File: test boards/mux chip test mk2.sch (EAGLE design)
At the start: 39 parts, among them IC1 741G3157DRLR, IC2 74AHC1G125DBV, IC3 741G3157DRLR, SW1 SPST_TACT-KMR2, U1 ATMEGA168MLF, Y1 16MHZ

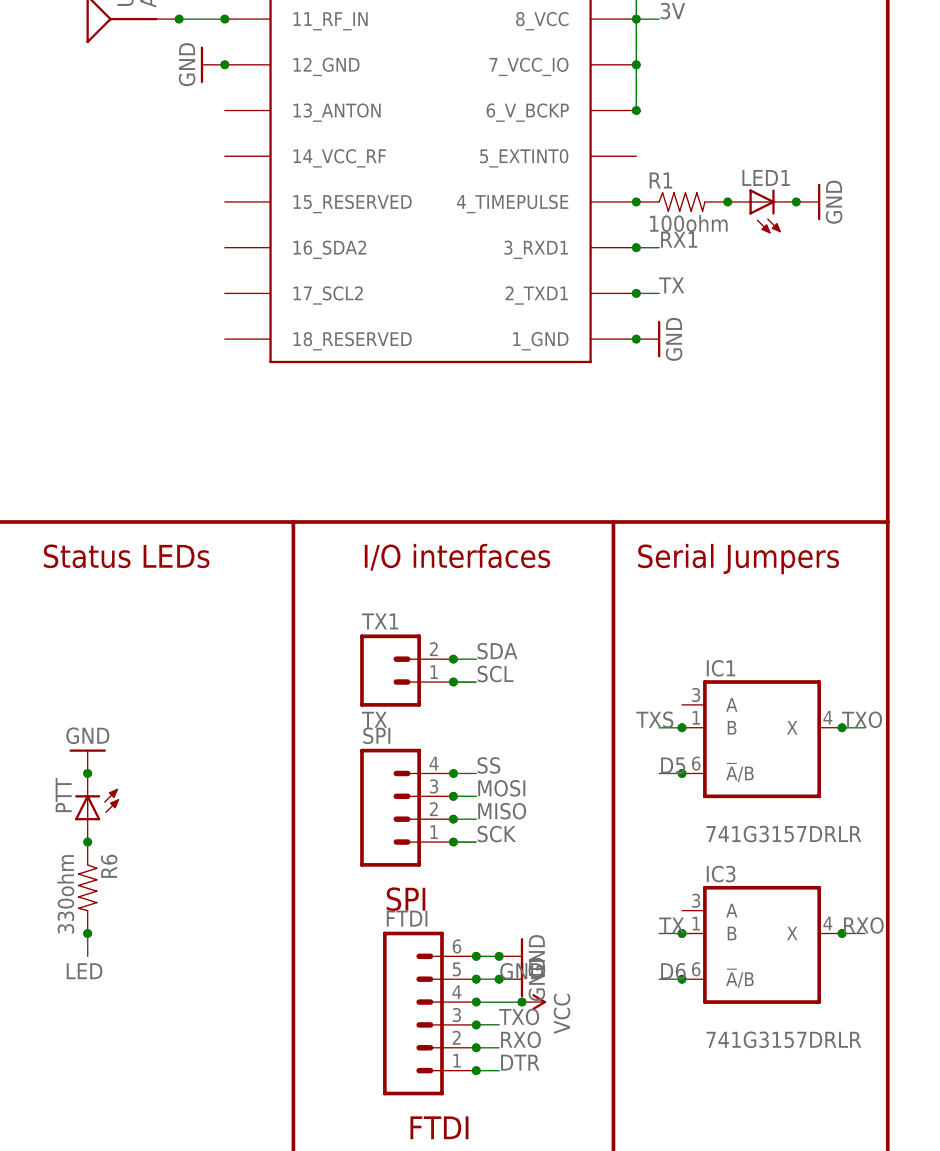
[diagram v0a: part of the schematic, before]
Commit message: Moved mix test LED
changed the schematic on the mux test to move the pulse per second LED
to the correct area on the schematic.
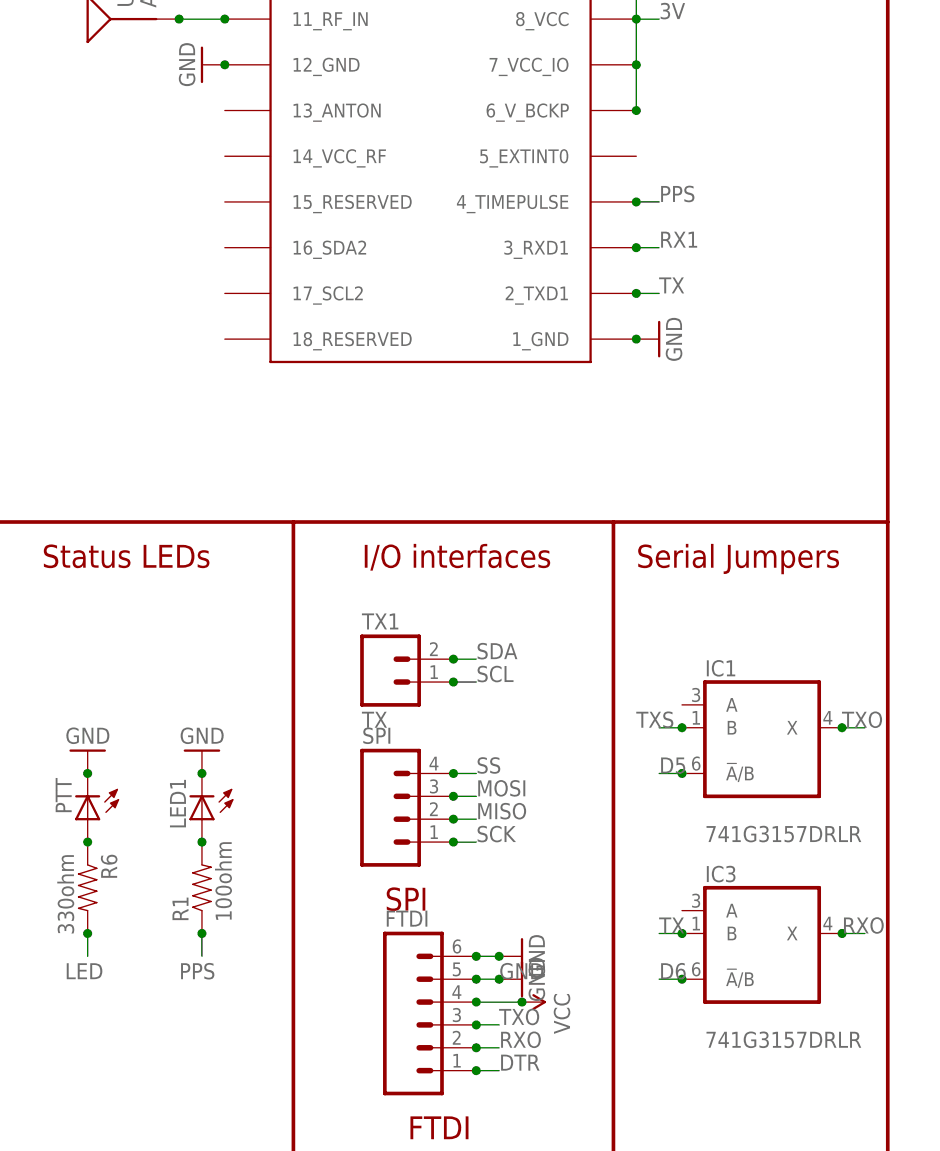
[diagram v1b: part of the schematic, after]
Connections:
- net N$2 renamed PPS
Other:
- moved on the sheet: LED1, R1
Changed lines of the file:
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@@
 <instance part="SUPPLY3" gate="G$1" x="109.22" y="132.08" rot="R90"/>
 <instance part="GND7" gate="1" x="106.68" y="127" rot="R270"/>
-<instance part="R1" gate="G$1" x="226.06" y="144.78"/>
-<instance part="LED1" gate="G$1" x="233.68" y="144.78" rot="R90"/>
-<instance part="GND8" gate="1" x="241.3" y="144.78" rot="R90"/>
+<instance part="R1" gate="G$1" x="172.72" y="68.58" rot="R90"/>
+<instance part="LED1" gate="G$1" x="172.72" y="76.2" rot="R180"/>
+<instance part="GND8" gate="1" x="172.72" y="83.82" rot="R180"/>
 <instance part="GND9" gate="1" x="223.52" y="129.54" rot="R90"/>
 <instance part="GND13" gate="1" x="172.72" y="160.02" rot="R270"/>
@@
 <pinref part="LED1" gate="G$1" pin="C"/>
 <pinref part="GND8" gate="1" pin="GND"/>
-<junction x="238.76" y="144.78"/>
+<junction x="172.72" y="81.28"/>
 </segment>
 <segment>
@@
 <pinref part="R1" gate="G$1" pin="2"/>
 <pinref part="LED1" gate="G$1" pin="A"/>
-<junction x="231.14" y="144.78"/>
+<junction x="172.72" y="73.66"/>
 </segment>
 </net>
@@
 <junction x="25.4" y="43.18"/>
 <pinref part="Y1" gate="G$1" pin="1"/>
-</segment>
-</net>
-<net name="N$2" class="0">
-<segment>
-<pinref part="U$1" gate="G$1" pin="4_TIMEPULSE"/>
-<pinref part="R1" gate="G$1" pin="1"/>
-<junction x="220.98" y="144.78"/>
 </segment>
 </net>
@@
 </segment>
 </net>
+<net name="PPS" class="0">
+<segment>
+<pinref part="R1" gate="G$1" pin="1"/>
+<wire x1="172.72" y1="63.5" x2="172.72" y2="60.96" width="0.1524" layer="91"/>
+<label x="170.18" y="58.42" size="1.778" layer="95"/>
+<junction x="172.72" y="63.5"/>
+</segment>
+<segment>
+<pinref part="U$1" gate="G$1" pin="4_TIMEPULSE"/>
+<wire x1="220.98" y1="144.78" x2="223.52" y2="144.78" width="0.1524" layer="91"/>
+<label x="223.52" y="144.78" size="1.778" layer="95"/>
+<junction x="220.98" y="144.78"/>
+</segment>
+</net>
